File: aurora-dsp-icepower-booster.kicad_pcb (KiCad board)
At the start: 2 copper layers, 158 x 200 mm, 268 parts, among them J1 24V DC, J10 XLR3_OUT, J11 XLR3_OUT, J12 XLR3_OUT, J13 XLR3_OUT, J14 XLR3_OUT, J2 REMOTE 3.5mm, J3 XLR_IN_1, J4 XLR_IN_2, J5 XLR_IN_3, J6 XLR_IN_4, J7 XLR_IN_5, J8 XLR_IN_6, J9 XLR3_OUT, Q1 BSS138, Q2 BSS138, Q3 BSS138, Q4 BSS138, Q5 BSS138, Q6 BSS138, Q7 BSS138, SW1 ALWAYS/REMOTE, SW2 Gain CH1, SW3 Gain CH2, SW4 Gain CH3, SW5 Gain CH4, SW6 Gain CH5, SW7 Gain CH6, U1 TEL5-2422, U10 LM4562, U11 LM4562, U12 LM4562, U13 LM4562, U14 ADP7118ARDZ-11, U15 ADP7182AUJZ-11, U2 LM4562, U3 LM4562, U4 LM4562, U5 LM4562, U6 LM4562, U7 LM4562, U8 LM4562, U9 LM4562

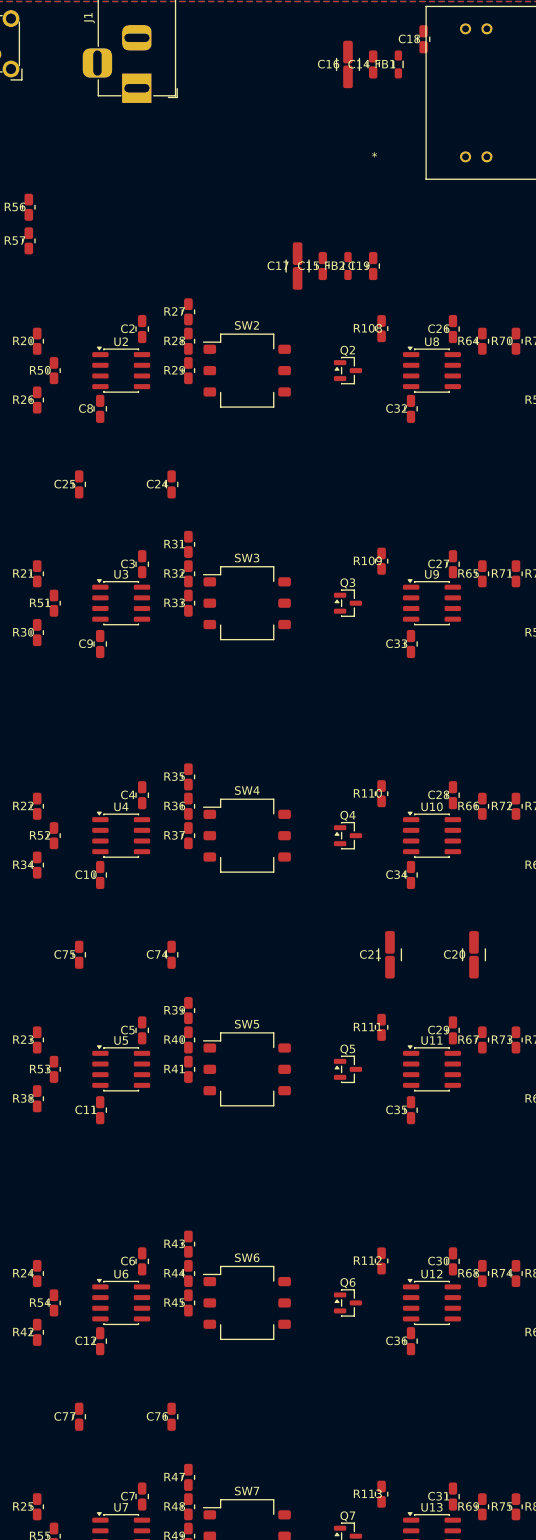
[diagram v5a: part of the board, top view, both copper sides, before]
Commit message: Fix alle 5 Audit-Fehler: TEL5 bypass, LDO-Handling, Driver bulk caps
Fehler 1 (U1 TEL5): C14/C15 an TEL5-Ausgangspins verschoben
  - C14 → (85, 34) = 2.2mm vom +12V_RAW Pin 14 (war 14.9mm)
  - C15 → (84.5, 19) = 2.6mm vom -12V_RAW Pin 11
  - Innerhalb U1 CrtYd — Standard-DIP-Bypass zwischen Pinreihen

Fehler 2 (U15 LDO): Audit für LDO-Regler angepasst
  - LDOs brauchen µF-Bypass statt nF → CHECK 1 relaxiert auf 6mm bulk
  - U15: C79 (10µF) @ 5.7mm → bestanden

Fehler 3-5 (U9/U12/U13 Driver): Bulk-Caps umverteilt
  - C20 → (108, 85) zwischen U9/U10 (11.8mm / 12.9mm)
  - C21 → (104, 141) zwischen U11/U12 (11.5mm / 13.3mm)
  - C77 → (104, 176) bei U13 (6.9mm)
  - Alle 6 Driver UND 6 Rx ICs innerhalb 20mm ✅

Audit: TEL5 DIP-24 Pin-Positionen hinzugefügt
Ergebnis: 0 Errors (von 5), 14 Warnings (akzeptabel)
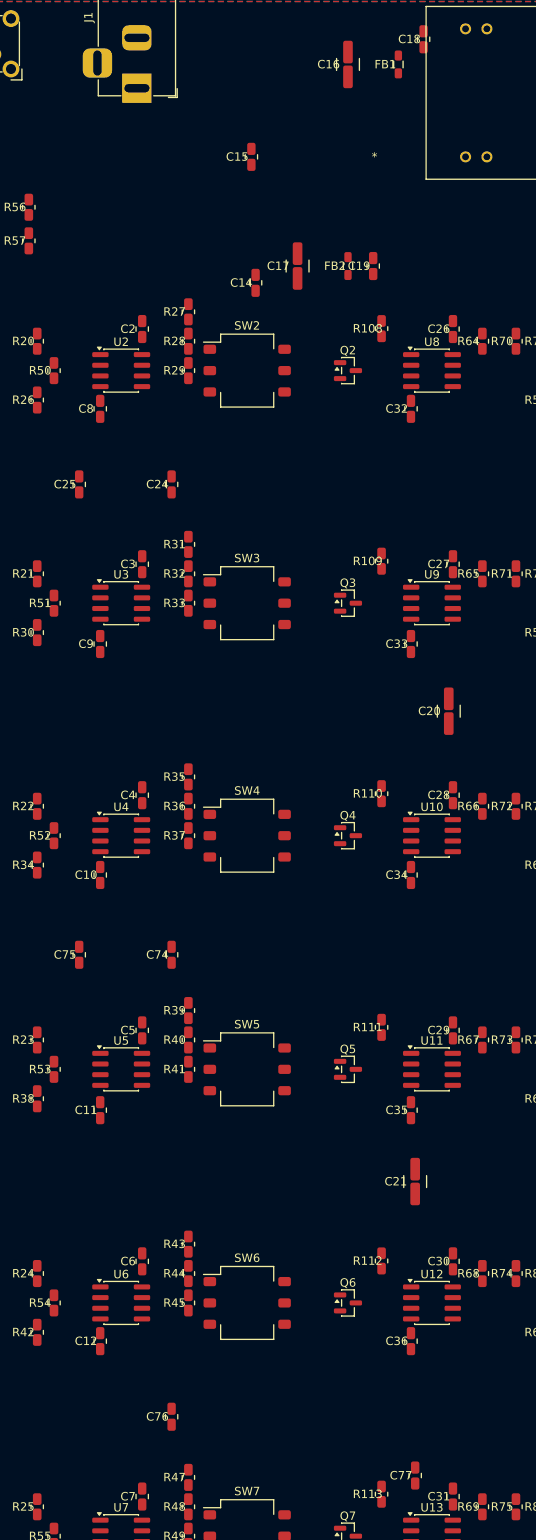
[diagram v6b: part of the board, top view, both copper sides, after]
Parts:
- moved C77 40.6 mm to (104.0, 176.0)
- moved C14 29.5 mm to (85.0, 34.0)
- moved C20 29.2 mm to (108.0, 85.0)
- moved C21 27.2 mm to (104.0, 141.0)
- moved C15 15.5 mm to (84.5, 19.0)
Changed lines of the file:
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@@
 	(footprint "Capacitor_SMD:C_0805_2012Metric"
 		(layer "F.Cu")
-		(at 99.0000 8.0000 90)
+		(at 85.0000 34.0000 90)
 		(descr "Capacitor SMD 0805 (2012 Metric), square (rectangular) end terminal, IPC-7351 nominal, (Body size source: IPC-SM-782 page 76, https://www.pcb-3d.com/wordpress/wp-content/uploads/ipc-sm-782a_amendment_1_and_2.pdf, https://docs.google.com/spreadsheets/d/1BsfQQcO9C6DZCsRaXUlFlo91Tg2WpOkGARC1WS5S8t0/edit?usp=sharing), generated with kicad-footprint-generator")
 		(tags "capacitor")
@@
 	(footprint "Capacitor_SMD:C_0805_2012Metric"
 		(layer "F.Cu")
-		(at 93.0000 32.0000 90)
+		(at 84.5000 19.0000 90)
 		(descr "Capacitor SMD 0805 (2012 Metric), square (rectangular) end terminal, IPC-7351 nominal, (Body size source: IPC-SM-782 page 76, https://www.pcb-3d.com/wordpress/wp-content/uploads/ipc-sm-782a_amendment_1_and_2.pdf, https://docs.google.com/spreadsheets/d/1BsfQQcO9C6DZCsRaXUlFlo91Tg2WpOkGARC1WS5S8t0/edit?usp=sharing), generated with kicad-footprint-generator")
 		(tags "capacitor")
@@
 	(footprint "Capacitor_SMD:C_1210_3225Metric"
 		(layer "F.Cu")
-		(at 111.0000 114.0000 90)
+		(at 108.0000 85.0000 90)
 		(descr "Capacitor SMD 1210 (3225 Metric), square (rectangular) end terminal, IPC-7351 nominal, (Body size source: IPC-SM-782 page 76, https://www.pcb-3d.com/wordpress/wp-content/uploads/ipc-sm-782a_amendment_1_and_2.pdf), generated with kicad-footprint-generator")
 		(tags "capacitor")
@@
 	(footprint "Capacitor_SMD:C_1210_3225Metric"
 		(layer "F.Cu")
-		(at 101.0000 114.0000 90)
+		(at 104.0000 141.0000 90)
 		(descr "Capacitor SMD 1210 (3225 Metric), square (rectangular) end terminal, IPC-7351 nominal, (Body size source: IPC-SM-782 page 76, https://www.pcb-3d.com/wordpress/wp-content/uploads/ipc-sm-782a_amendment_1_and_2.pdf), generated with kicad-footprint-generator")
 		(tags "capacitor")
@@
 	(footprint "Capacitor_SMD:C_0805_2012Metric"
 		(layer "F.Cu")
-		(at 64.0000 169.0000 90)
+		(at 104.0000 176.0000 90)
 		(descr "Capacitor SMD 0805 (2012 Metric), square (rectangular) end terminal, IPC-7351 nominal, (Body size source: IPC-SM-782 page 76, https://www.pcb-3d.com/wordpress/wp-content/uploads/ipc-sm-782a_amendment_1_and_2.pdf, https://docs.google.com/spreadsheets/d/1BsfQQcO9C6DZCsRaXUlFlo91Tg2WpOkGARC1WS5S8t0/edit?usp=sharing), generated with kicad-footprint-generator")
 		(tags "capacitor")

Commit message: Validierung: Netzklassen-Zuweisungen, DRU, Silkscreen
- 71 Netz→Netzklasse Zuweisungen in .kicad_pro:
  Power (5): +12V, -12V, +12V_RAW, -12V_RAW, +24V_IN
  Audio_Input (18): CHn_INV_IN, CHn_EMI_HOT/COLD
  Audio_Output (48): CHn_OUT_DRIVE, CHn_BUF_DRIVE, CHn_GAIN_FB etc.
- DRU: audio_power_width Regel hinzugefügt (≥0.5mm)
- PCB: Board-Info Silkscreen auf B.SilkS (Projektname + Rev 1.0)
- Alle via_diameter korrekt konfiguriert (0.6-0.8mm je Klasse)
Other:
- board text added: "Aurora DSP IcePower Booster"
- board text added: "Rev 1.0"
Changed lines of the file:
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@@
 		)
 	)
+	(gr_text "Aurora DSP IcePower Booster" (at 30.0 197.0) (layer "B.SilkS") (effects (font (size 1.2 1.2) (thickness 0.15))))
+	(gr_text "Rev 1.0" (at 30.0 199.0) (layer "B.SilkS") (effects (font (size 1.2 1.2) (thickness 0.15))))
 )

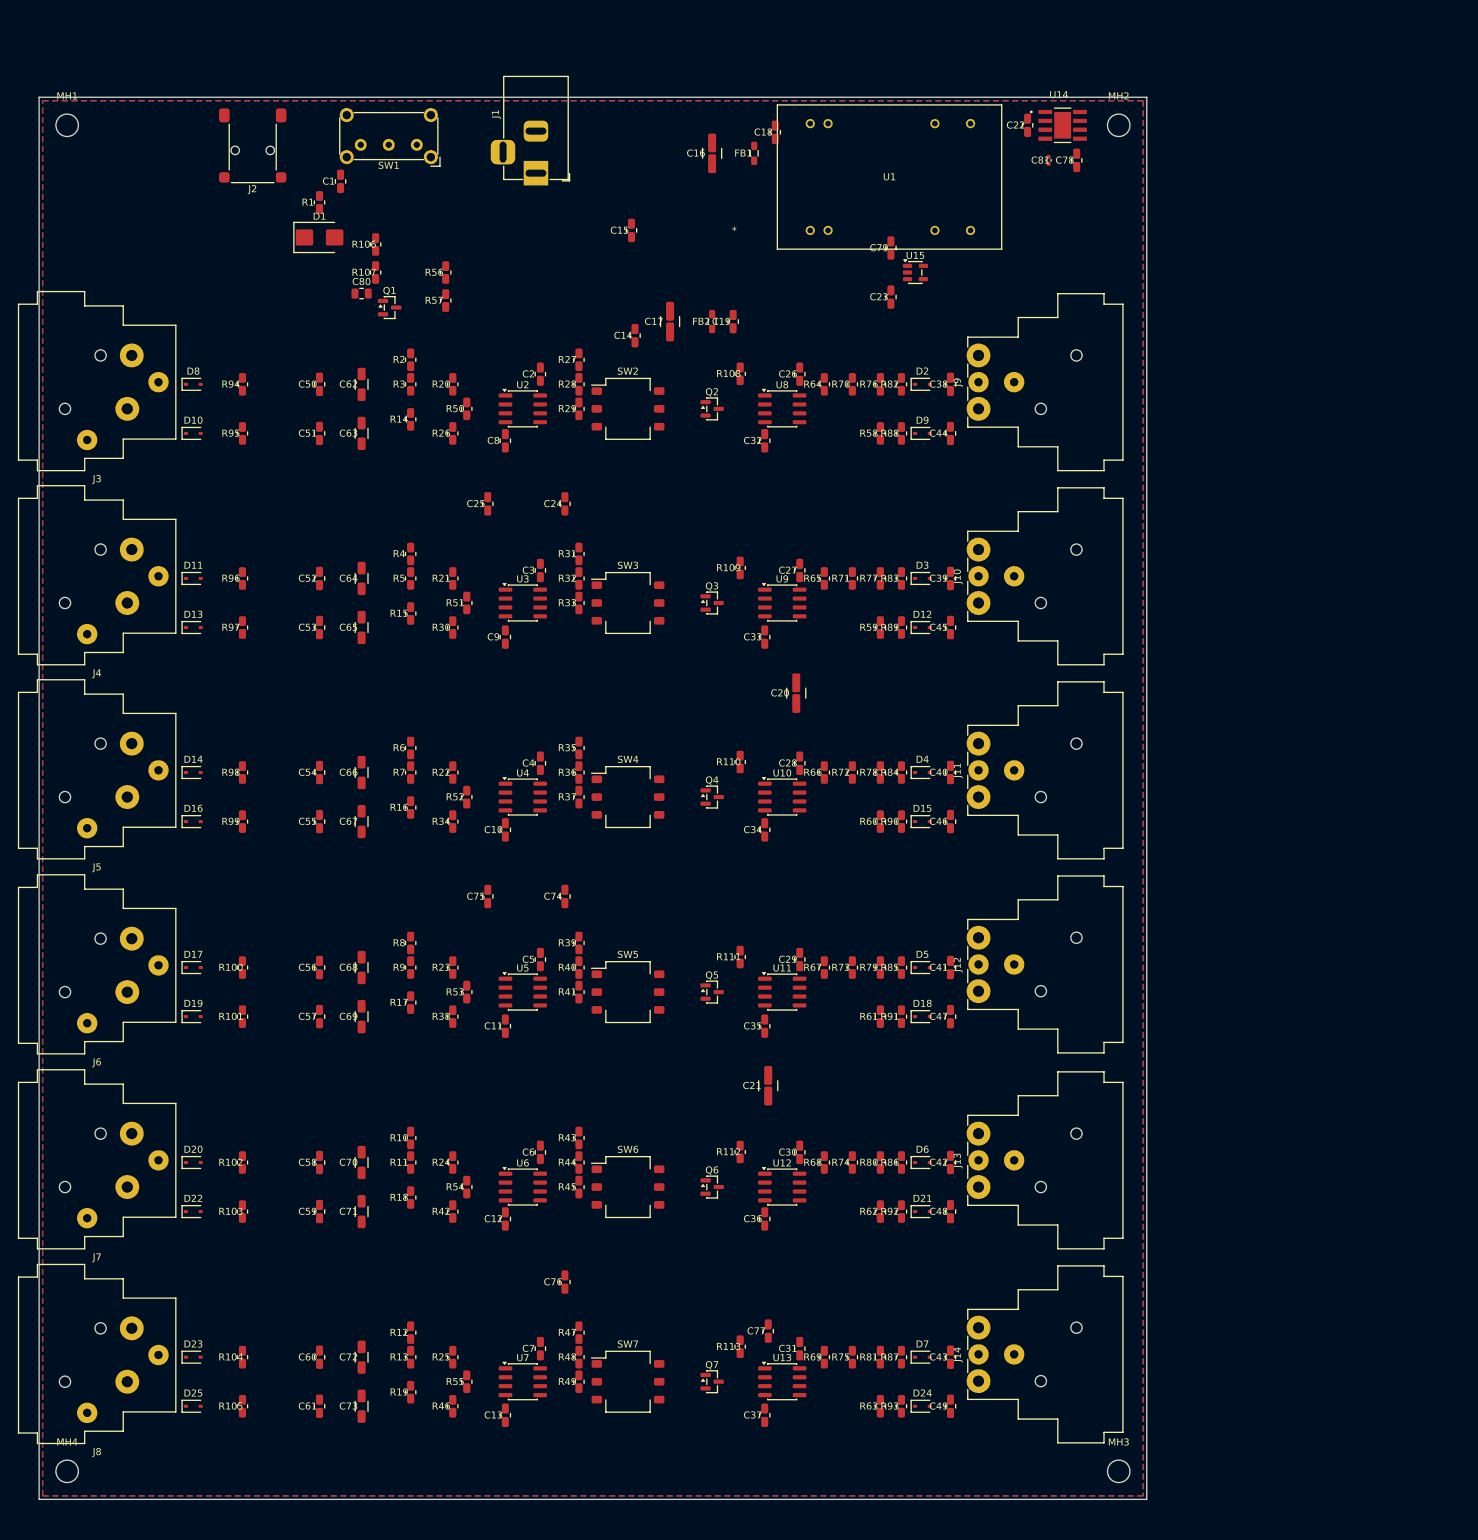
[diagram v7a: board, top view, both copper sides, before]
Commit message: Routing: Freerouting autoroute + zone fill + production export
- Netclass clearances aligned with DRU rules:
  - Power: 0.2mm → 0.25mm (matches power_clearance DRU)
  - HV netclass added: 0.5mm clearance for +24V_IN
  - Net patterns updated (+24V_IN, +24V* → HV class)
- Freerouting v2.0.1: 6 passes, 1276 segments + 138 vias
- 6 DSN netclasses: Audio_Input(48), Audio_Output(66), Audio_Power(2),
  Default(19), HV(1), Power(5/GND)
- Zone fill: 2 GND zones (F.Cu + B.Cu) filled via pcbnew API
- DRC: 2 errors (known courtyard overlaps C18/C79 on U1),
  0 clearance violations, 16 GND zone islands (F.Cu)
- Production files re-exported: Gerber (9 layers), drill, BOM, pos
- Routing pipeline scripts: route_1..6 + DSN netclass fixer
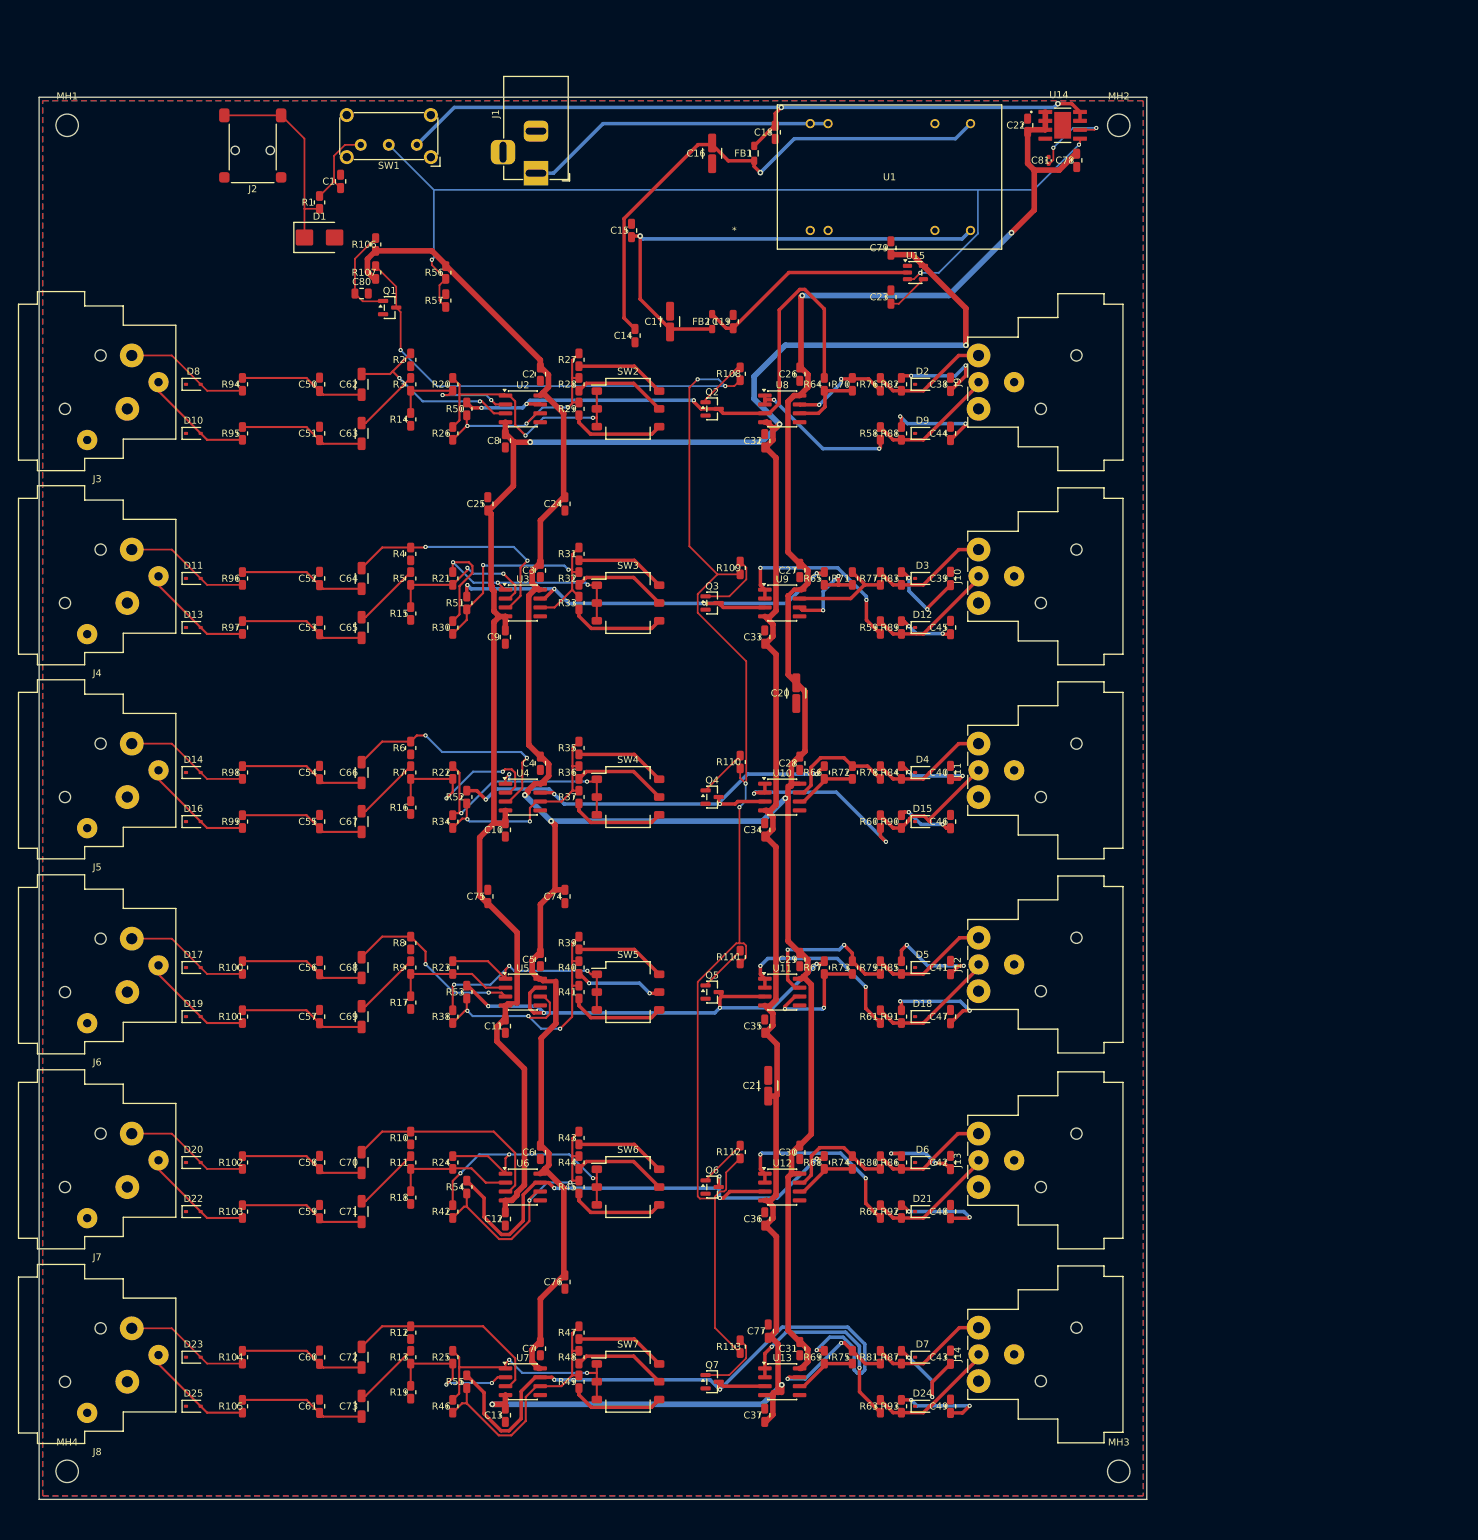
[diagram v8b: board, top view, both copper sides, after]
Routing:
- net /V+: track 0.00 -> 468.0 mm, vias 0 -> 5
- net /V-: track 0.00 -> 437.8 mm, vias 0 -> 5
- net /MUTE: track 0.00 -> 237.9 mm, vias 0 -> 5
- net /EN_CTRL: track 0.00 -> 142.1 mm, vias 0 -> 3
- net /+12V: track 0.00 -> 105.9 mm, vias 0 -> 2
- net /CH6_GAIN_OUT: track 0.00 -> 97.2 mm, vias 0 -> 3
- net /CH1_GAIN_OUT: track 0.00 -> 80.8 mm, vias 0 -> 3
- net /+12V_RAW: track 0.00 -> 75.4 mm, vias 0 -> 1
- net /CH5_GAIN_OUT: track 0.00 -> 75.3 mm, vias 0 -> 4
- net /CH4_GAIN_OUT: track 0.00 -> 70.7 mm, vias 0 -> 4
- net /-12V_RAW: track 0.00 -> 70.6 mm, vias 0 -> 1
- net /CH2_GAIN_OUT: track 0.00 -> 67.4 mm, vias 0 -> 4
- net /CH3_GAIN_OUT: track 0.00 -> 65.2 mm, vias 0 -> 4
- net /+24V_IN: track 0.00 -> 44.6 mm
- net /CH5_RX_OUT: track 0.00 -> 43.6 mm, vias 0 -> 3
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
